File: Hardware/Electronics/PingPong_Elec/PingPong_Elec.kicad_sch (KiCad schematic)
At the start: 0 parts

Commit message: added symbols
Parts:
- added M1, M4, M5: Motor_Servo, symbol Motor:Motor_Servo
- added M2, M6: ~, symbol Motors:Motor_BLDC_3Phase
- added M3, M7, M8: ~, symbol Motors:Motor_Gear_DC
- added U1, U7, U8: ~, symbol Motor_Drivers:DRV8871_DC_Motor_Driver
- added U2: ~, symbol PWM_Drivers:PCA9685PW
- added U3: ~, symbol Power_Modules:BUCK_XL4016
- added U4: ~, symbol Wireless_Modules:HC05
- added U6: STM32F103RBTx, Package_QFP:LQFP-64_10x10mm_P0.5mm, symbol MCU_ST_STM32F1:STM32F103RBTx
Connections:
- new net: U6.18 (VSS), U6.31 (VSS), U6.47 (VSS), U6.63 (VSS)
- new net GND: M1.3 (-), M4.3 (-), M5.3 (-)
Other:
- note added: "Bluetooth"
- note added: "Brushless"
- note added: "Buck Converter"
- note added: "Gear Motor Driver"
- note added: "Geared"
- note added: "Servo Controller"
- note added: "Servos"

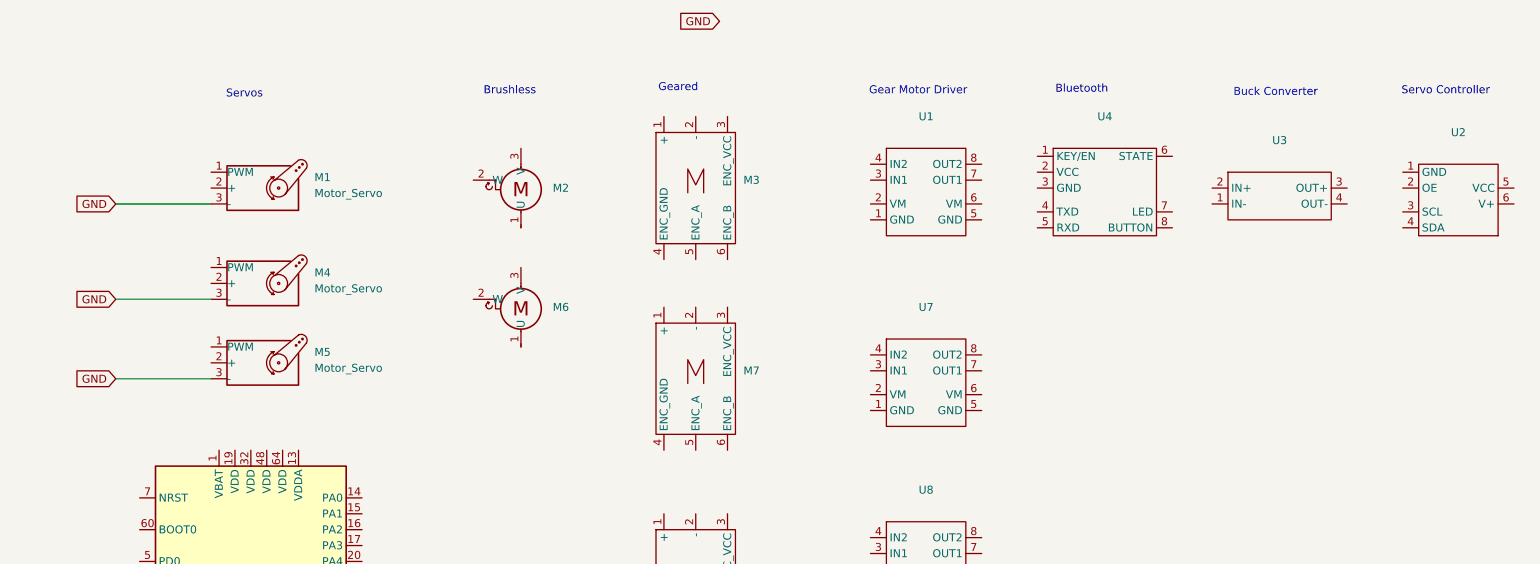
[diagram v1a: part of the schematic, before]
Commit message: semi wired servos
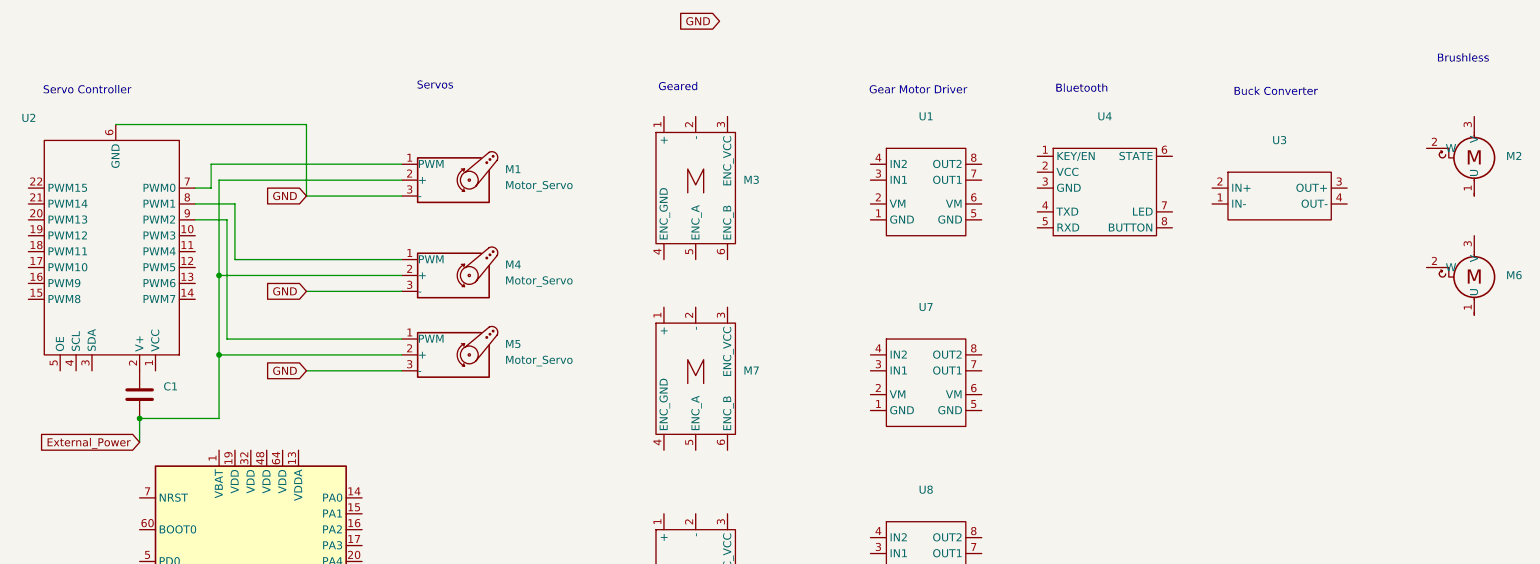
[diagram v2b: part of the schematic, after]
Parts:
- removed U2: ~, symbol PWM_Drivers:PCA9685PW
- added C1: C, symbol Device:C
- added U2: ~, symbol PWM_Driver:PCA9685PW_Module
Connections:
- net GND: now also U2.6 (GND)
- net at M1.1 (PWM): now also U2.7 (PWM0)
- net External_Power: now reaches M1.2 (+)
- net External_Power: now also M4.2 (+), M5.2 (+), C1.2
- net at M4.1 (PWM): now also U2.8 (PWM1)
- net at M5.1 (PWM): now also U2.9 (PWM2)
- new net: C1.1, U2.2 (V+)
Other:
- moved on the sheet: M1, M2, M4, M5, M6

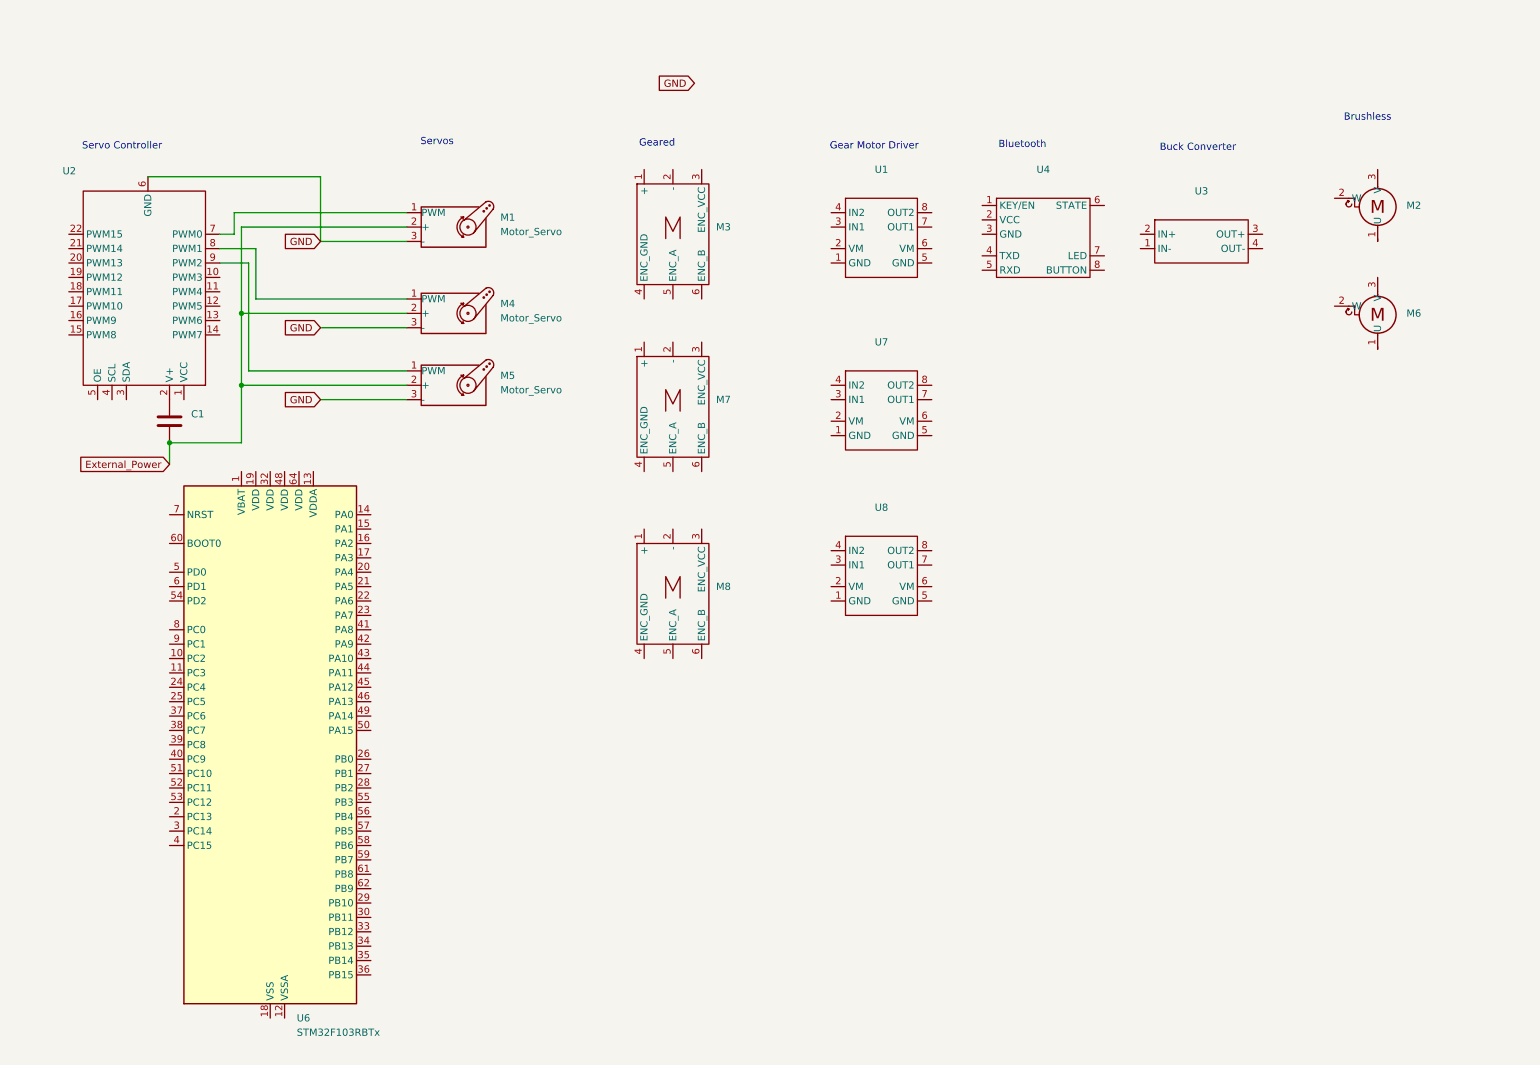
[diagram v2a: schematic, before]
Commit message: wiring for servo and geared motors
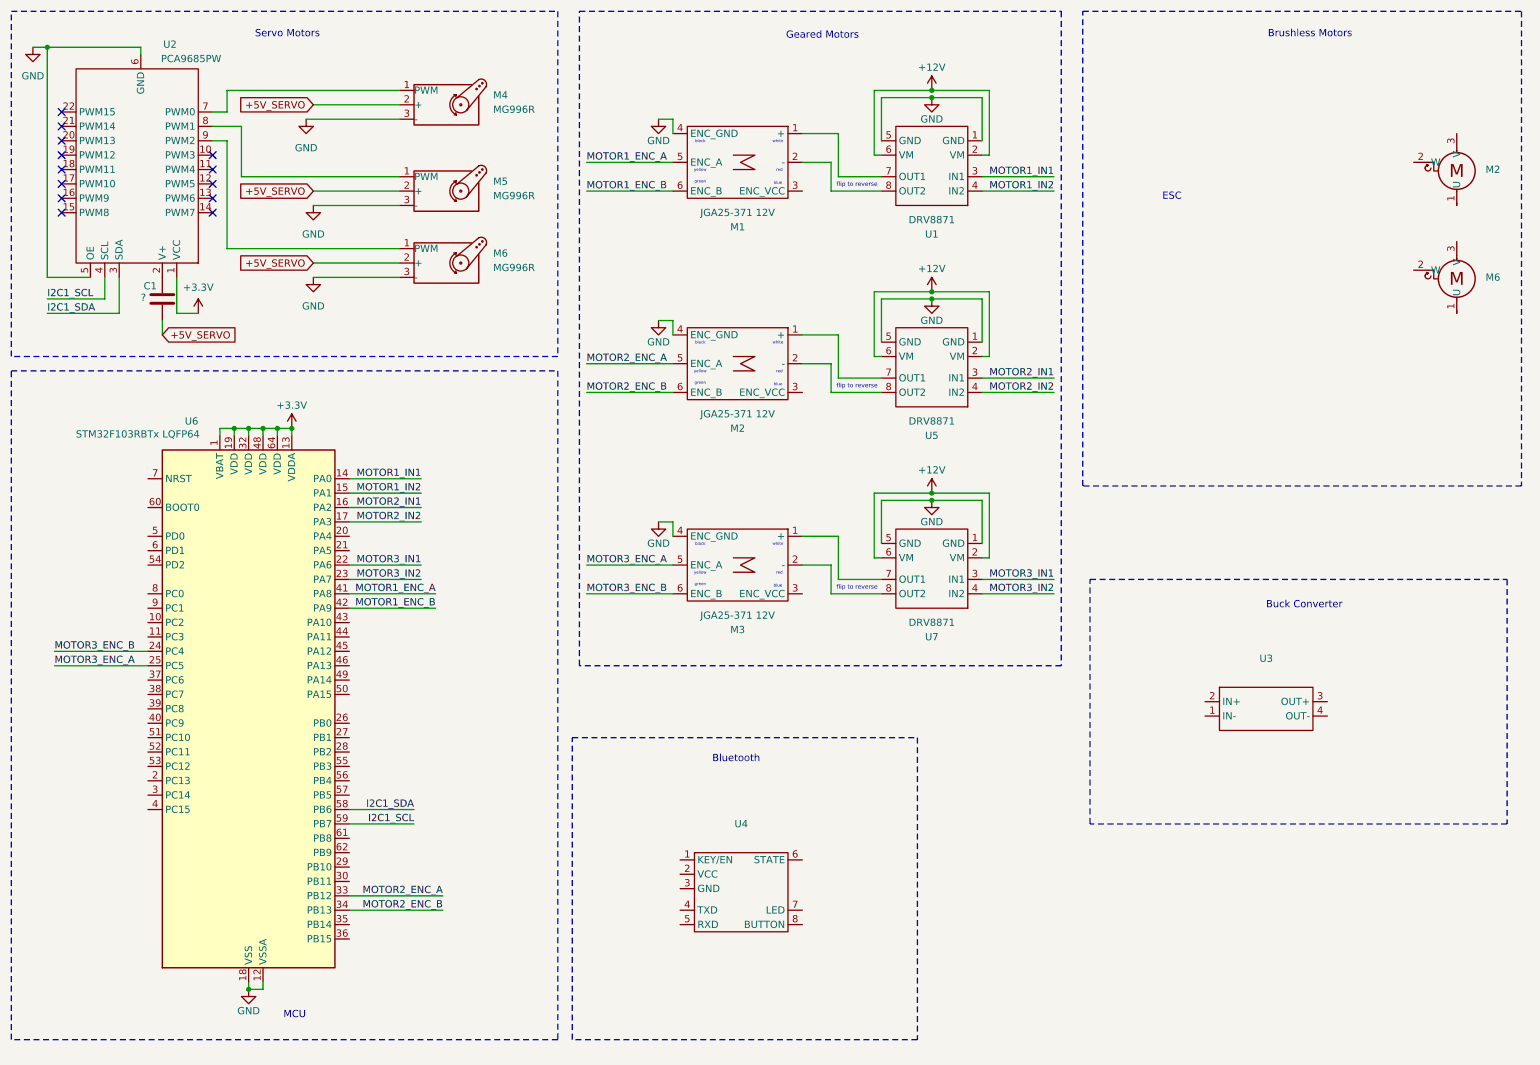
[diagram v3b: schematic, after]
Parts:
- removed M7, M8: ~, symbol Motors:Motor_Gear_DC
- removed U8: ~, symbol Motor_Drivers:DRV8871_DC_Motor_Driver
- added M2, M3: JGA25-371 12V, symbol Motors:Motor_Gear_DC
- added U5: DRV8871, symbol Motor_Drivers:DRV8871_DC_Motor_Driver
- C1: value C -> ?
- M1: renamed from M3; value ~ -> JGA25-371 12V
- M4: renamed from M1; value Motor_Servo -> MG996R
- M5: renamed from M4; value Motor_Servo -> MG996R
- M6: renamed from M5; value Motor_Servo -> MG996R
- U1, U7: value ~ -> DRV8871
- U2: value ~ -> PCA9685PW
- U6: value STM32F103RBTx -> STM32F103RBTx LQFP64
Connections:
- net GND: now also M1.4 (ENC_GND), U1.1 (GND), U1.5 (GND), U2.5 (OE), U6.12 (VSSA), U6.18 (VSS), U6.31 (VSS), U6.47 (VSS), U6.63 (VSS), U7.1 (GND), U7.5 (GND), M2.4 (ENC_GND), M3.4 (ENC_GND), U5.1 (GND), U5.5 (GND)
- net at M1.1 (+): now also U1.7 (OUT1)
- net at M1.2 (-): now also U1.8 (OUT2)
- net MOTOR1_ENC_A: now reaches M1.5 (ENC_A)
- net MOTOR1_ENC_A: now also U6.41 (PA8)
- net MOTOR1_ENC_B: now reaches M1.6 (ENC_B)
- net MOTOR1_ENC_B: now also U6.42 (PA9)
- net +12V: now reaches U7.2 (VM)
- net +12V: now also U1.2 (VM), U1.6 (VM), U7.6 (VM), U5.2 (VM), U5.6 (VM)
- net MOTOR3_IN1: now reaches U7.3 (IN1)
- net MOTOR3_IN1: now also U6.22 (PA6)
- net MOTOR3_IN2: now reaches U7.4 (IN2)
- net MOTOR3_IN2: now also U6.23 (PA7)
- net at U7.7 (OUT1): now also M3.1 (+)
- net at U7.8 (OUT2): now also M3.2 (-)
- net +3.3V: now reaches U2.1 (VCC)
- net +3.3V: now also U6.1 (VBAT), U6.13 (VDDA), U6.19 (VDD), U6.32 (VDD), U6.48 (VDD), U6.64 (VDD)
- net I2C1_SDA: now reaches U2.3 (SDA)
- net I2C1_SDA: now also U6.58 (PB6)
- net I2C1_SCL: now reaches U2.4 (SCL)
- net I2C1_SCL: now also U6.59 (PB7)
- net MOTOR1_IN1: now reaches U1.3 (IN1)
- net MOTOR1_IN1: now also U6.14 (PA0)
- net MOTOR1_IN2: now reaches U1.4 (IN2)
- net MOTOR1_IN2: now also U6.15 (PA1)
- net MOTOR2_IN1: now reaches U6.16 (PA2)
- net MOTOR2_IN1: now also U5.3 (IN1)
- net MOTOR2_IN2: now reaches U6.17 (PA3)
- net MOTOR2_IN2: now also U5.4 (IN2)
- net MOTOR3_ENC_B: now reaches U6.24 (PC4)
- net MOTOR3_ENC_B: now also M3.6 (ENC_B)
- net MOTOR3_ENC_A: now reaches U6.25 (PC5)
- net MOTOR3_ENC_A: now also M3.5 (ENC_A)
- net MOTOR2_ENC_A: now reaches U6.33 (PB12)
- net MOTOR2_ENC_A: now also M2.5 (ENC_A)
- net MOTOR2_ENC_B: now reaches U6.34 (PB13)
- net MOTOR2_ENC_B: now also M2.6 (ENC_B)
- net External_Power renamed +5V_SERVO
- new net: M2.1 (+), U5.7 (OUT1)
- new net: M2.2 (-), U5.8 (OUT2)
- no-connect marks 0 -> 13
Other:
- note added: "Brushless Motors"
- note added: "ESC"
- note added: "Geared Motors"
- note added: "MCU"
- note added: "Servo Motors"
- note added: "black"
- note added: "blue"
- note added: "flip to reverse"
- note added: "green"
- note added: "red"
- note added: "white"
- note added: "yellow"
- note removed: "Brushless"
- note removed: "Gear Motor Driver"
- note removed: "Geared"
- note removed: "Servo Controller"
- note removed: "Servos"
- title: (none) -> PongServer Schematic
- moved on the sheet: C1, M1, M2, M4, M5, M6, U1, U2, U3, U4, U6

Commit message: wired all schematic diagrams, adding bypass and decoupling caps
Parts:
- removed M6: ~, symbol Motors:Motor_BLDC_3Phase
- added BT1, BT2, BT3, BT4, BT5, BT6: 11.1V, symbol Device:Battery
- added C1, C11, C4, C6, C8, C9: 0.1 µF, symbol Device:C
- added C10, C12: 2.2 mF, symbol Device:C
- added C3, C5, C7: 1 mF, symbol Device:C
- added M8: A2212/6T 2200KV, symbol Motors:Motor_BLDC_3Phase
- added R1: 100kR, symbol Device:R_Small_US
- added U6, U7: 30A ESC, symbol Motors:3Phase_ESC
- C2: renamed from C1; value ? -> 1 mF
- M7: renamed from M2; value ~ -> A2212/6T 2200KV
- U8: renamed from U3; value ~ -> 300W XL4016
- U9: renamed from U4; value ~ -> HC-05 OG RS232
- renumbered M4 to M1, M5 to M2, M6 to M3, M1 to M4, M2 to M5, M3 to M6, U6 to U1, U1 to U3, U5 to U4, U7 to U5
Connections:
- net +5V_SERVO is gone; now on net +5V_DIST: C2.2, M1.2 (+), M2.2 (+), M3.2 (+)
- net GND: now also C2.1, U8.1 (IN-), U8.4 (OUT-), U9.3 (GND), BT4.2 (-), BT5.2 (-), BT6.2 (-), C1.1, C10.2, C11.1, C12.2, C3.1, C4.1, C5.1, C6.1, C7.1, C8.1, C9.1, R1.2, U6.5 (GND), U6.8 (GND), U7.5 (GND), U7.8 (GND)
- net at U9.1 (KEY/EN): now also R1.1
- net +5V_DEV: now reaches U9.2 (VCC)
- net BT_RX: now reaches U9.4 (TXD)
- net BT_RX: now also U1.30 (PB11)
- net BT_TX: now reaches U9.5 (RXD)
- net BT_TX: now also U1.29 (PB10)
- net +5V_DIST: now reaches U2.2 (V+)
- net +5V_DIST: now also U8.3 (OUT+), C1.2; no longer C2.1
- net at U8.2 (IN+): now also BT6.1 (+)
- net at M7.1 (U): now also U6.1 (U)
- net at M7.2 (W): now also U6.3 (W)
- net at M7.3 (V): now also U6.2 (V)
- net MOTOR7_PWM: now reaches U1.43 (PA10)
- net MOTOR7_PWM: now also U6.6 (PWM)
- net MOTOR8_PWM: now reaches U1.44 (PA11)
- net MOTOR8_PWM: now also U7.6 (PWM)
- removed net +12V: U3.2 (VM), U3.6 (VM), U4.2 (VM), U4.6 (VM), U5.2 (VM), U5.6 (VM)
- net MOTOR1_ENC_A renamed MOTOR4_ENC_A
- net MOTOR1_ENC_B renamed MOTOR4_ENC_B
- net MOTOR1_IN1 renamed MOTOR4_IN1
- net MOTOR1_IN2 renamed MOTOR4_IN2
- net MOTOR2_ENC_A renamed MOTOR5_ENC_A
- net MOTOR2_ENC_B renamed MOTOR5_ENC_B
- net MOTOR2_IN1 renamed MOTOR5_IN1
- net MOTOR2_IN2 renamed MOTOR5_IN2
- net MOTOR3_ENC_A renamed MOTOR6_ENC_A
- net MOTOR6_ENC_A: now also U1.24 (PC4); no longer U1.25 (PC5)
- net MOTOR3_ENC_B renamed MOTOR6_ENC_B
- net MOTOR6_ENC_B: now also U1.25 (PC5); no longer U1.24 (PC4)
- net MOTOR3_IN1 renamed MOTOR6_IN1
- net MOTOR3_IN2 renamed MOTOR6_IN2
- new net: BT2.1 (+), U4.2 (VM), U4.6 (VM)
- new net: BT3.2 (-), C7.2, C8.2
- new net: BT5.1 (+), C11.2, C12.1, U7.7 (VBAT)
- new net: BT2.2 (-), C5.2, C6.2
- new net: BT1.1 (+), U3.2 (VM), U3.6 (VM)
- new net: BT1.2 (-), C3.2, C4.2
- new net: BT3.1 (+), U5.2 (VM), U5.6 (VM)
- new net: M8.1 (U), U7.1 (U)
- new net: M8.2 (W), U7.3 (W)
- new net: M8.3 (V), U7.2 (V)
- new net: BT4.1 (+), C10.1, C9.2, U6.7 (VBAT)
- no-connect marks 13 -> 53
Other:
- note added: "AT cmd mode for configuration pull-up if needed"
- note added: "LED and Button are already on the board"
- note added: "Power output to MCU Only connect if STM not powered by micro USB"
- note removed: "ESC"
- moved on the sheet: C2, M1, M2, M3, M4, M5, M6, M7, U1, U2, U3, U4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

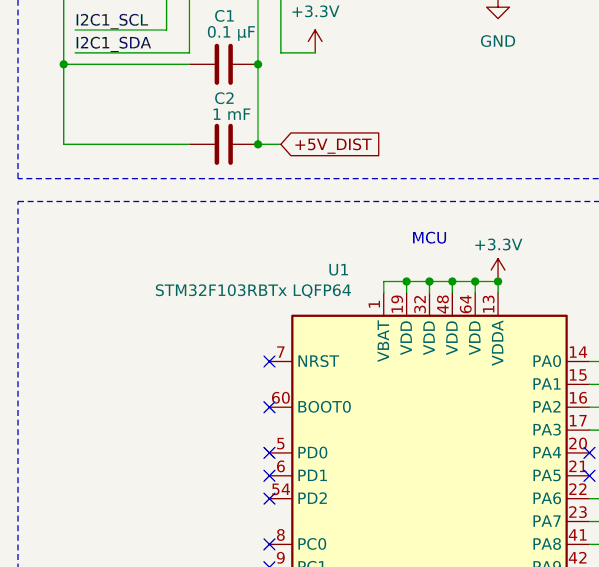
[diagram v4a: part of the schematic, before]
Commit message: fixed names for MCU
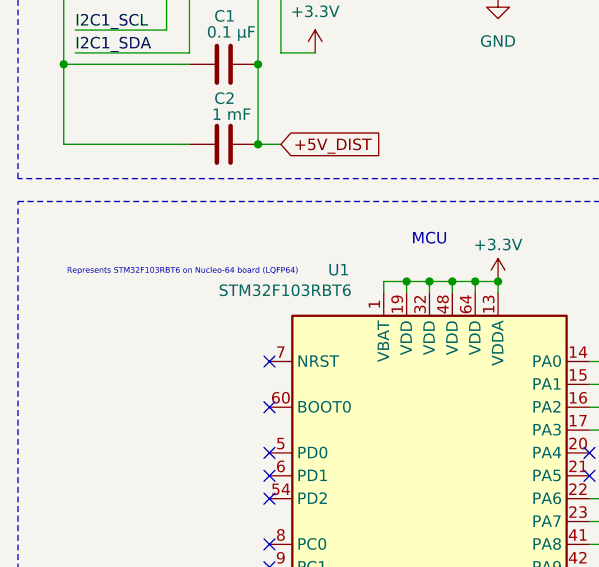
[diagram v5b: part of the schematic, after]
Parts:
- U1: value STM32F103RBTx LQFP64 -> STM32F103RBT6
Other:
- note added: "Represents STM32F103RBT6 on Nucleo-64 board (LQFP64)"
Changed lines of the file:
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@@
 		)
 	)
+	(text "Represents STM32F103RBT6 on Nucleo-64 board (LQFP64)"
+		(exclude_from_sim no)
+		(at 32.258 90.424 0)
+		(effects
+			(font
+				(size 0.635 0.635)
+			)
+		)
+	)
 	(text "Servo Motors"
 		(exclude_from_sim no)
@@
 			)
 		)
-		(property "Value" "STM32F103RBTx LQFP64"
+		(property "Value" "STM32F103RBT6"
 			(at 51.054 92.456 0)
 			(effects
